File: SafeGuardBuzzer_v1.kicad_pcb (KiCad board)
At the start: 2 copper layers, 90 x 45 mm, 16 parts, among them J1 SWD_DEBUG, J2 VBAT_GND_TEST, Q1 AO3400A, U1 DA14531MOD-00F01002

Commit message: Checkpoint before Buzzer CR2450 redesign
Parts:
- BT1: value BH-123A-A1CJ002 -> Keystone 3008 CR2450; footprint SafeGuardBuzzer_Local:BatteryHolder_CR123A_MYOUNG_BH-123A-A1CJ002_C5290177_THT -> BatteryHolder_Keystone_3008_1x2450; moved to B.Cu
- moved BT1 1.00 mm to (28.0, 27.0)
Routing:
- net VBAT_RAW: track 63.7 -> 122.8 mm, vias 0 -> 3
- net GND: track 244.0 -> 262.8 mm, vias 9 -> 10

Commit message: Redesign Buzzer v1 for CR2450 battery
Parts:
- BT1: value Keystone 3008 CR2450 -> MYOUNG MY-2450-03 CR2450 holder; footprint BatteryHolder_Keystone_3008_1x2450 -> SafeGuardBuzzer_Local:BatteryHolder_MYOUNG_MY-2450-03_C2988622_CR2450
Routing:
- net VBAT_RAW: track 122.8 -> 116.2 mm
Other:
- board size 90 x 45 mm -> 88.8 x 45 mm

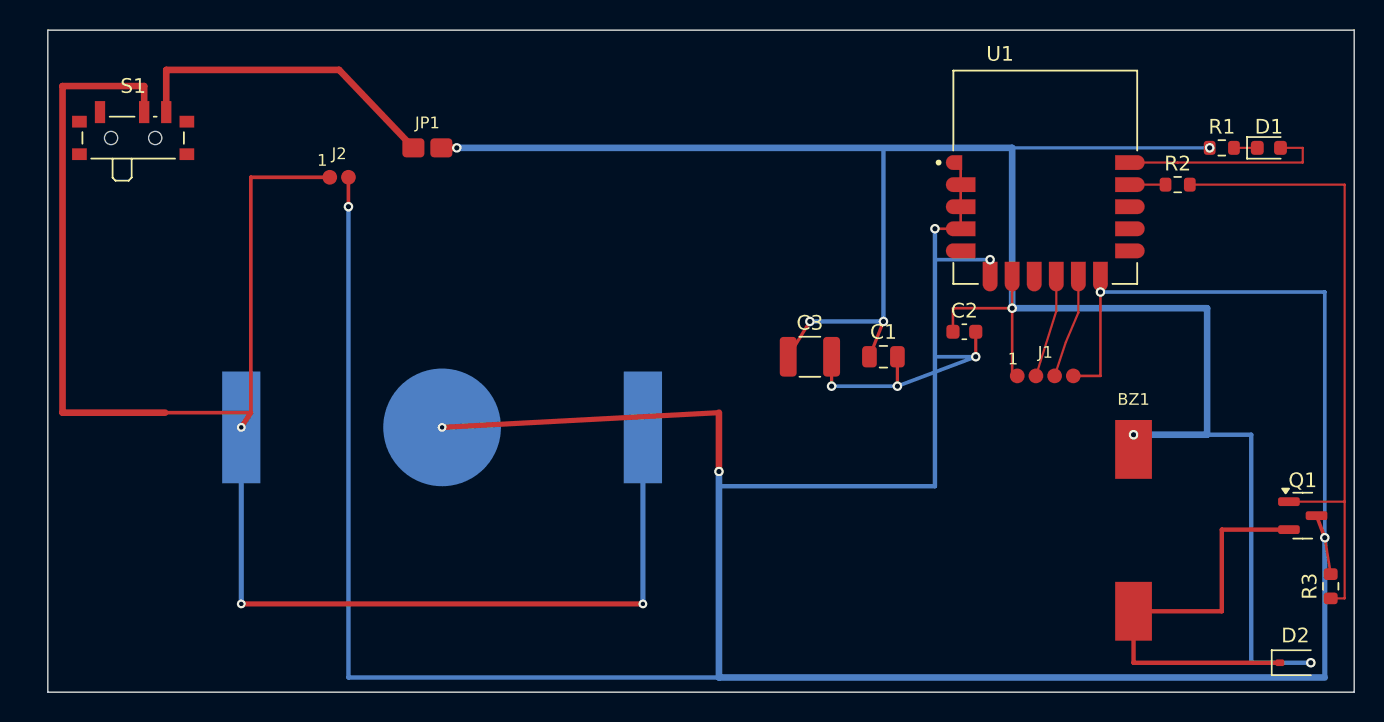
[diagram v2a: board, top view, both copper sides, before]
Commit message: Convert Buzzer CR2450 to one-sided assembly
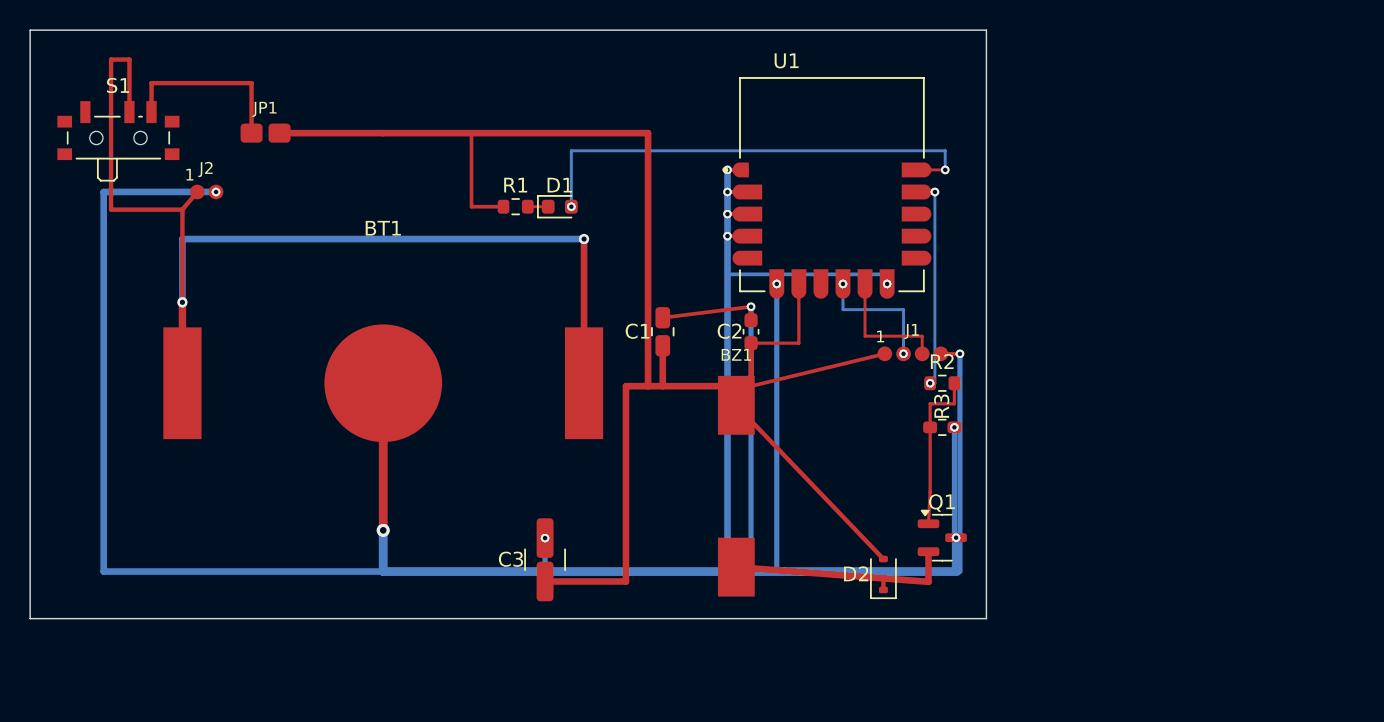
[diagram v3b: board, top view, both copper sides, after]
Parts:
- BT1: moved to F.Cu
- moved D1 48.4 mm to (36.0, 12.0)
- moved R1 48.2 mm to (33.0, 12.0)
- moved D2 28.6 mm to (58.0, 37.0), turned to 90 degrees
- moved R3 28.5 mm to (62.0, 27.0), turned to 0 degrees
- moved BZ1 27.2 mm to (48.0, 31.0)
- moved Q1 24.5 mm to (62.0, 34.5)
- moved C3 22.7 mm to (35.0, 36.0), turned to 90 degrees
- moved R2 20.9 mm to (62.0, 24.0)
- moved C1 15.1 mm to (43.0, 20.5), turned to 90 degrees
- moved U1 14.5 mm to (54.5, 10.5)
- moved C2 14.5 mm to (49.0, 20.5), turned to 90 degrees
- moved JP1 11.0 mm to (16.0, 7.00)
- moved J1 9.12 mm to (60.0, 22.0)
- moved J2 9.06 mm to (12.0, 11.0)
- moved BT1 5.00 mm to (24.0, 24.0)
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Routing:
- net VBAT_RAW: track 116.2 -> 74.6 mm, vias 3 -> 2
- net GND: track 262.8 -> 223.4 mm, vias 10 -> 13
- net VCC: track 153.4 -> 115.1 mm, vias 7 -> 0
- net BUZZER_PWM_GATE: track 43.4 -> 11.2 mm
- net LED_STATUS: track 14.3 -> 32.5 mm, vias 0 -> 2
- net BUZZER_NEG: track 29.6 -> 15.9 mm
- net BUZZER_PWM: track 2.42 -> 14.6 mm, vias 0 -> 2
- net VBAT_SW: track 21.9 -> 12.2 mm
- net SWDIO: track 6.96 -> 8.87 mm, vias 0 -> 2
- net SWCLK: track 7.05 -> 8.63 mm
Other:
- board size 88.8 x 45 mm -> 65 x 40 mm

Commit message: PCB contains copper zones near C3; fixed it
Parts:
- C3: footprint Capacitor_SMD:C_1210_3225Metric -> SafeGuardBuzzer_Local:C_1210_3225_Samsung_CL32A107MQVNNNE_C49066
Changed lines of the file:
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@@
 		)
 	)
-	(footprint "Capacitor_SMD:C_1210_3225Metric"
+	(footprint "SafeGuardBuzzer_Local:C_1210_3225_Samsung_CL32A107MQVNNNE_C49066"
 		(layer "F.Cu")
 		(at 35 36 90)
-		(descr "Capacitor SMD 1210 (3225 Metric), square (rectangular) end terminal, IPC-7351 nominal, (Body size source: IPC-SM-782 page 76, https://www.pcb-3d.com/wordpress/wp-content/uploads/ipc-sm-782a_amendment_1_and_2.pdf), generated with kicad-footprint-generator")
-		(tags "capacitor")
+		(descr "Samsung CL32A107MQVNNNE / LCSC C49066, nonpolar 100uF 6.3V X5R MLCC. Body 3.20x2.50x2.50mm, termination BW 0.60+/-0.30mm from Samsung. Pads 1.635x2.700mm on 3.035mm pitch from official JLC/LCSC EasyEDA package C1210 for C49066.")
+		(tags "capacitor MLCC 1210 3225 Samsung CL32A107MQVNNNE C49066")
 		(property "Reference" "C3"
-			(at 0 -2.3 0)
+			(at 0 -2.3 90)
 			(layer "F.SilkS")
 			(effects
@@
 		)
 		(property "Value" "100uF"
-			(at 0 2.3 0)
+			(at 0 2.3 90)
 			(layer "F.Fab")
 			(effects
@@
 		)
 		(property "Datasheet" ""
-			(at 0 0 0)
+			(at 0 0 90)
 			(layer "F.Fab")
 			(hide yes)
@@
 		)
 		(property "Description" ""
-			(at 0 0 0)
+			(at 0 0 90)
 			(layer "F.Fab")
 			(hide yes)
@@
 		(attr smd)
 		(fp_line
-			(start -0.711252 -1.36)
-			(end 0.711252 -1.36)
+			(start -0.6 -1.36)
+			(end 0.6 -1.36)
 			(stroke
 				(width 0.12)
@@
 		)
 		(fp_line
-			(start -0.711252 1.36)
-			(end 0.711252 1.36)
+			(start -0.6 1.36)
+			(end 0.6 1.36)
 			(stroke
 				(width 0.12)
@@
 			(layer "F.SilkS")
 		)
-		(fp_line
-			(start -2.3 -1.6)
-			(end 2.3 -1.6)
+		(fp_rect
+			(start -2.6 -1.65)
+			(end 2.6 1.65)
 			(stroke
 				(width 0.05)
 				(type solid)
 			)
+			(fill no)
 			(layer "F.CrtYd")
 		)
-		(fp_line
-			(start -2.3 1.6)
-			(end -2.3 -1.6)
-			(stroke
-				(width 0.05)
-				(type solid)
-			)
-			(layer "F.CrtYd")
-		)
-		(fp_line
-			(start 2.3 -1.6)
-			(end 2.3 1.6)
-			(stroke
-				(width 0.05)
-				(type solid)
-			)
-			(layer "F.CrtYd")
-		)
-		(fp_line
-			(start 2.3 1.6)
-			(end -2.3 1.6)
-			(stroke
-				(width 0.05)
-				(type solid)
-			)
-			(layer "F.CrtYd")
-		)
-		(fp_line
+		(fp_rect
 			(start -1.6 -1.25)
-			(end 1.6 -1.25)
-			(stroke
-				(width 0.1)
-				(type solid)
-			)
-			(layer "F.Fab")
-		)
-		(fp_line
-			(start -1.6 1.25)
-			(end -1.6 -1.25)
-			(stroke
-				(width 0.1)
-				(type solid)
-			)
-			(layer "F.Fab")
-		)
-		(fp_line
-			(start 1.6 -1.25)
 			(end 1.6 1.25)
 			(stroke
@@
 				(type solid)
 			)
-			(layer "F.Fab")
-		)
-		(fp_line
-			(start 1.6 1.25)
-			(end -1.6 1.25)
-			(stroke
-				(width 0.1)
-				(type solid)
-			)
+			(fill no)
 			(layer "F.Fab")
 		)
 		(fp_text user "${REFERENCE}"
-			(at 0 0 0)
+			(at 0 0 90)
 			(layer "F.Fab")
 			(effects
@@
 			)
 		)
-		(pad "1" smd roundrect
-			(at -1.475 0)
-			(size 1.15 2.7)
-			(layers "F.Cu" "F.Mask" "F.Paste")
-			(roundrect_rratio 0.217391)
+		(pad "1" smd rect
+			(at -1.5175 0 90)
+			(size 1.635 2.7)
+			(layers "F.Cu" "F.Paste" "F.Mask")
 			(net 11 "VCC")
 		)
-		(pad "2" smd roundrect
-			(at 1.475 0)
-			(size 1.15 2.7)
-			(layers "F.Cu" "F.Mask" "F.Paste")
-			(roundrect_rratio 0.217391)
+		(pad "2" smd rect
+			(at 1.5175 0 90)
+			(size 1.635 2.7)
+			(layers "F.Cu" "F.Paste" "F.Mask")
 			(net 4 "GND")
 		)
